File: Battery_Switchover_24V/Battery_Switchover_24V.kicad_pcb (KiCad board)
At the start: 4 copper layers, 198.6 x 89 mm, 194 parts, among them J1 USB_C_Receptacle_USB2.0_14P, J10 ATX_2X3, J11 ATX_2X3, J12 ATX_2X3, J13 ATX_2X3, J14 M6, J15 M6, J2 M8, J4 M8, J5 M8, J6 Conn_01x08, J7 Conn_01x05, J8 ATX_2X3, J9 ATX_2X3, M1 Fan, Q1 PZT2222AT1G, Q10 FDBL86066-F085, Q11 BC817, Q2 PJD50N10AL_L2, Q3 PJD50N10AL_L2, Q4 FDBL86066-F085, Q5 FDBL86066-F085, Q6 FDBL86066-F085, Q7 FDBL86066-F085, Q8 FDBL86066-F085, Q9 FDBL86066-F085, SW1 SW_Push, SW2 SW_Push, SW3 SW_Push, U1 LM25117PSQE_NOPB, U10 LPC11U67JBD48, U12 L5973D, U13 AMS1117-3.3, U14 OPA2197xD, U15 IRS21867S, U16 LM74610QDGKRQ1, U17 IRS21867S, U18 LM60CIM3_NOPB, U2 ACS71240LLCBTR-010B3, U3 IRS21867S, U4 ACS71240LLCBTR-010B3, U5 ACS71240LLCBTR-010B3, U6 LM74610QDGKRQ1, U7 ACS71240LLCBTR-010B3, U8 ADS7830IPWR, U9 LMV321

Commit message: Board turned to horizontal
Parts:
- removed C14: 10uF, Capacitor_SMD:C_1206_3216Metric
- removed C15: 100nF, Capacitor_SMD:C_1206_3216Metric
- removed C28: 330uF, Capacitor_SMD:CP_Elec_8x10
- removed C45: 100nF, Capacitor_SMD:C_0603_1608Metric
- added C67: 10uF 50V X7R, Capacitor_SMD:C_1206_3216Metric, F.Cu at (92.8, 98.3)
- added C68: 10uF 16V X7R, Capacitor_SMD:C_1206_3216Metric, F.Cu at (99.7, 74.4)
- added C69: 10uF 16V X7R, Capacitor_SMD:C_1206_3216Metric, F.Cu at (102.1, 74.4)
- added C70: 10uF 50V X7R, Capacitor_SMD:C_1206_3216Metric, F.Cu at (231.5, 134.6)
- added C71: 10uF 50V X7R, Capacitor_SMD:C_1206_3216Metric, F.Cu at (228.2, 134.6)
- added C72: 10uF 50V X7R, Capacitor_SMD:C_1206_3216Metric, F.Cu at (224.8, 134.6)
- added C73: 10uF 50V X7R, Capacitor_SMD:C_1206_3216Metric, F.Cu at (221.4, 134.6)
- added J3: Conn_01x03, Connector_Phoenix_MC:PhoenixContact_MCV_1,5_3-G-3.5_1x03_P3.50mm_Vertical, F.Cu at (162.2, 155.4)
- BZ1, D16, D2, D4, D5, J2, J4, J5: moved to F.Cu
- C33: value 1nF -> 10uF 50V X7R; footprint Capacitor_SMD:C_0402_1005Metric -> Capacitor_SMD:C_1206_3216Metric
- C34: value 10nF -> 10uF 50V X7R; footprint Capacitor_SMD:C_0603_1608Metric -> Capacitor_SMD:C_1206_3216Metric
- C35: value 100nF -> 10uF 50V X7R; footprint Capacitor_SMD:C_0603_1608Metric -> Capacitor_SMD:C_1206_3216Metric
- C36: value 1nF -> 100nF
- C37, C38: footprint Capacitor_SMD:C_0402_1005Metric -> Capacitor_SMD:C_0603_1608Metric
- C39: value 100nF -> 100nF 16V; footprint Capacitor_SMD:C_0603_1608Metric -> Capacitor_SMD:C_1206_3216Metric
- C41: value 100nF -> 10uF 16V X7R; footprint Capacitor_SMD:C_0603_1608Metric -> Capacitor_SMD:C_1206_3216Metric
- C42: footprint Capacitor_SMD:C_0603_1608Metric -> Capacitor_SMD:C_0805_2012Metric
- C9: footprint Capacitor_SMD:C_0603_1608Metric -> Capacitor_SMD:C_1206_3216Metric
- DS1: footprint LCD_OLED_I2C:LCD_OLED_128X64_1.3_I2C -> Connector_PinSocket_2.54mm:PinSocket_1x04_P2.54mm_Vertical
- J1: footprint USB_C_Vertical:GCT_USB4145-03-0170-C_REVA2 -> Connector_USB:USB_C_Receptacle_HRO_TYPE-C-31-M-12; moved to F.Cu
- J6: footprint TerminalBlock_Phoenix:TerminalBlock_Phoenix_PT-1,5-8-3.5-H_1x08_P3.50mm_Horizontal -> Connector_Phoenix_MC:PhoenixContact_MCV_1,5_8-G-3.5_1x08_P3.50mm_Vertical
- M1: footprint TerminalBlock_Phoenix:TerminalBlock_Phoenix_PT-1,5-2-3.5-H_1x02_P3.50mm_Horizontal -> Connector_Phoenix_MC:PhoenixContact_MCV_1,5_2-G-3.5_1x02_P3.50mm_Vertical
- SW1, SW2, SW3: footprint Button_Switch_SMD:SW_SPST_TL3305A -> Button_Switch_THT:SW_Tactile_SPST_Angled_PTS645Vx58-2LFS; moved to F.Cu
- moved C41 317.7 mm to (97.2, 74.3)
- moved C39 311.3 mm to (112.8, 74.5), turned to 90 degrees
- moved C36 307.4 mm to (120.0, 73.5)
- moved R18 307.2 mm to (91.1, 88.0)
- moved C35 299.7 mm to (92.8, 95.9)
- moved C33 297.1 mm to (98.0, 98.3), turned to 180 degrees
- moved C34 293.6 mm to (98.0, 95.9), turned to 180 degrees
- moved C38 288.6 mm to (100.2, 86.7)
- moved C37 285.8 mm to (100.2, 88.3)
- moved C42 281.5 mm to (115.4, 73.2), turned to 180 degrees
- moved R19 271.3 mm to (91.0, 91.8)
- moved U13 267.8 mm to (119.1, 79.8)
- moved R17 251.0 mm to (100.2, 90.0)
- moved D10 238.7 mm to (92.3, 81.2), turned to 90 degrees
- moved C32 227.2 mm to (105.9, 95.5)
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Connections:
- C41 pad 1: +5V -> GND
- C41 pad 2: GND -> +5V
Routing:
- net VOUT: track 394.1 -> 149.3 mm
- net VIN: track 56.7 -> 24.0 mm
- net VBATT: track 45.4 -> 21.0 mm
- net GND: track 9.65 -> 0.00 mm
- net Net-(Q2-S): track 10.5 -> 6.59 mm
- removed copper zone on F.Cu, net VBATT
- removed copper zone on B.Cu, net VOUT
- removed copper zone on F.Cu, net VOUT
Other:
- board size 198.6 x 89 mm -> 198.6 x 104.2 mm

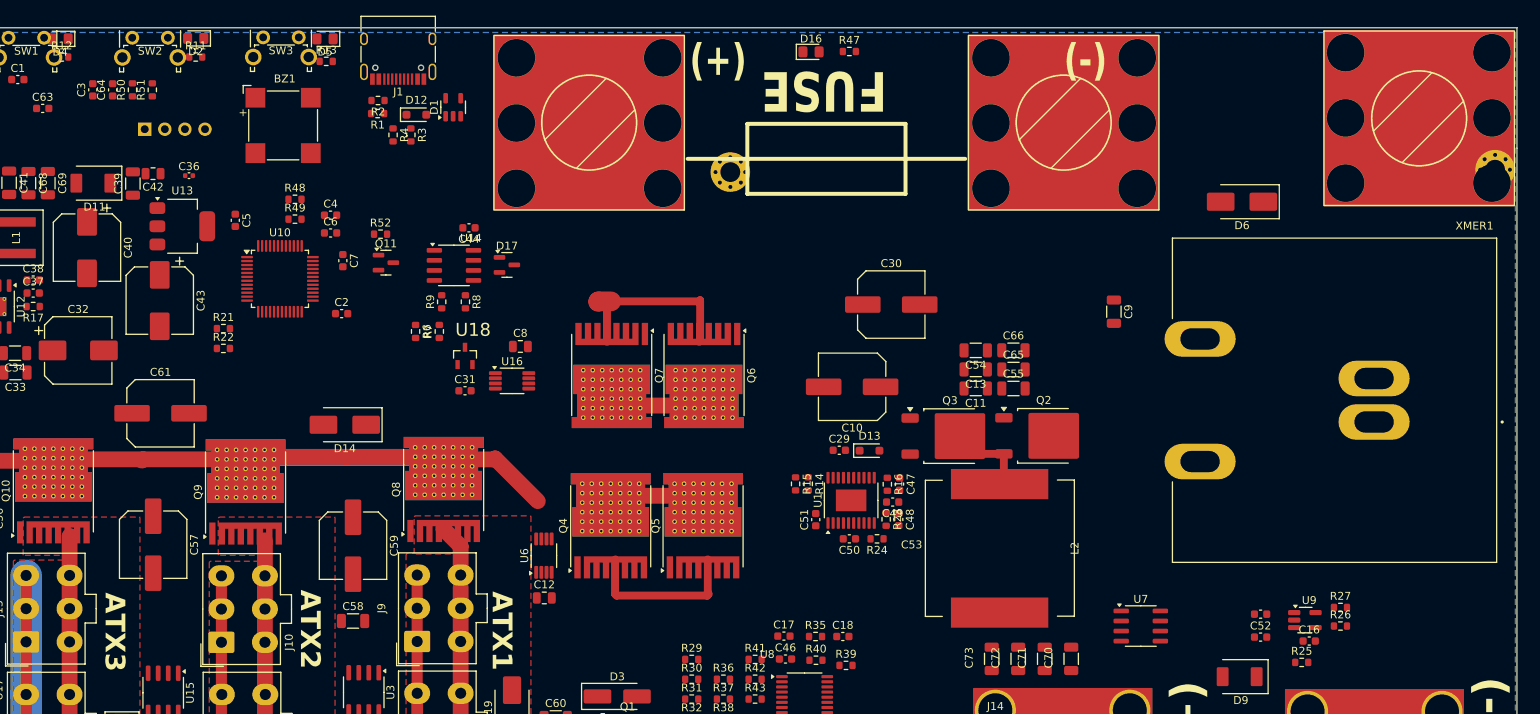
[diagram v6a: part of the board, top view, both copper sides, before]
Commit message: hiside load switch revised
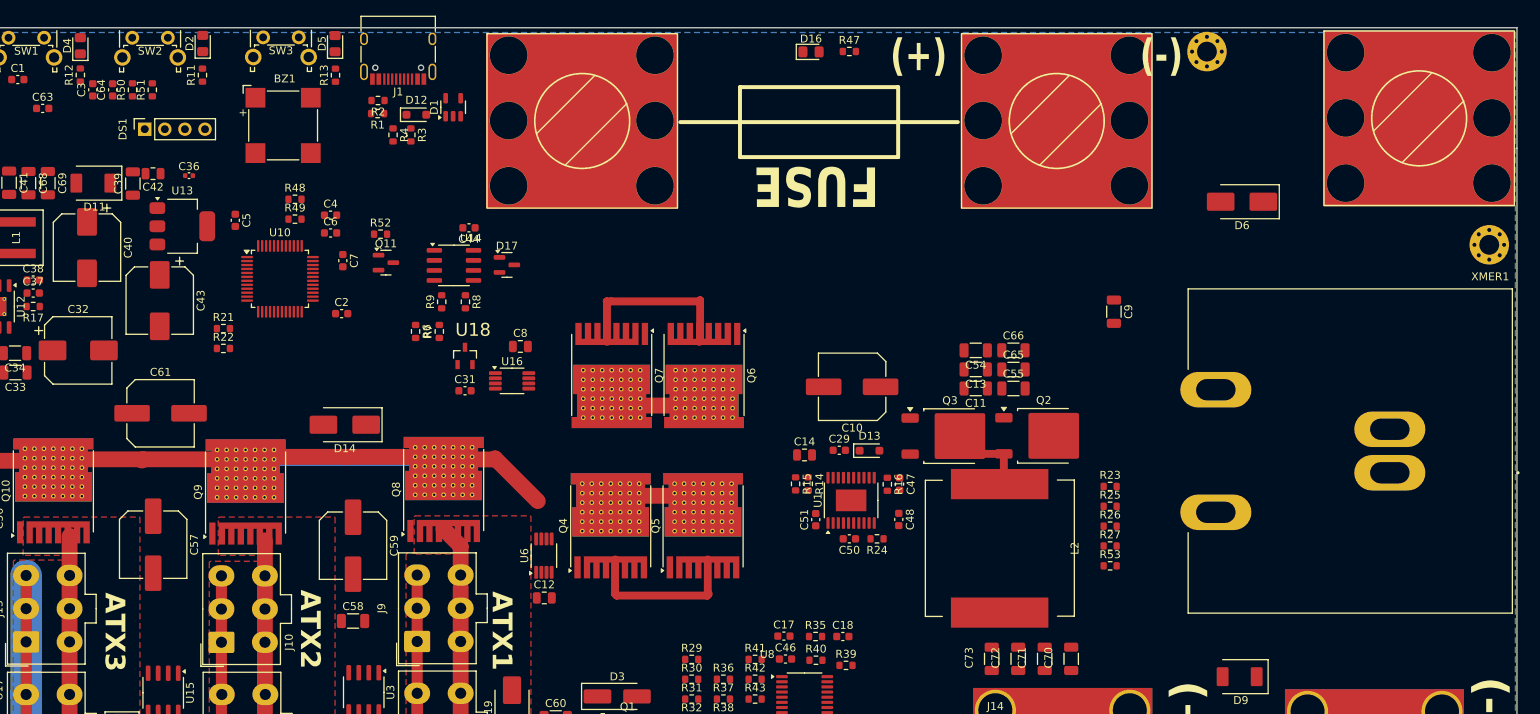
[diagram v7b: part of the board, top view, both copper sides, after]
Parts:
- removed C16, C49, C53: 100nF, Capacitor_SMD:C_0603_1608Metric
- removed C30: 330uF, Capacitor_SMD:C_Elec_8x10.2
- removed C52: 6nF, Capacitor_SMD:C_0603_1608Metric
- removed U7: ACS71240LLCBTR-010B3, Package_SO:SOIC-8_3.9x4.9mm_P1.27mm
- removed U9: LMV321, Package_TO_SOT_SMD:SOT-23-5_HandSoldering
- added C14: 1uF, Capacitor_SMD:C_0805_2012Metric, F.Cu at (197.8, 108.8)
- added R53: 5mOhm, Resistor_SMD:R_0603_1608Metric, F.Cu at (236.4, 122.8)
- C29, C50: value 100nF -> 0.47uF
- C47: value 100nF -> 1500pF
- C48: value 100nF -> 0.022uF
- DS1: moved to F.Cu
- R14, R16: value 7.5K -> 100K
- R15: value 7.5K -> 15K
- R23, R26: value 7.5K -> 3.24K
- R24: value 7.5K -> 22.1K
- R25: value 7.5K -> 2.37K
- R27: value 7.5K -> 332R
- moved J5 81.2 mm to (160.4, 58.2), turned to 0 degrees
- moved H6 62.2 mm to (248.7, 57.8)
- moved J2 43.9 mm to (220.4, 58.2), turned to 0 degrees
- moved R26 31.7 mm to (236.4, 117.8)
- moved R25 31.2 mm to (236.4, 115.3)
- moved R27 30.1 mm to (236.4, 120.3)
- moved R23 28.6 mm to (236.4, 112.8), turned to 0 degrees
- moved H4 9.52 mm to (284.4, 82.2)
- moved XMER1 6.72 mm to (266.8, 108.3)
- moved R12 3.28 mm to (106.2, 60.7), turned to 90 degrees
- moved D4 2.71 mm to (106.2, 57.0), turned to 90 degrees
- moved R11 2.44 mm to (121.7, 60.7), turned to 90 degrees
- moved R13 2.11 mm to (138.5, 60.8), turned to 90 degrees
- moved D5 1.41 mm to (138.4, 56.8), turned to 90 degrees
- moved D2 1.09 mm to (121.7, 56.7), turned to 90 degrees
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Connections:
- C29 pad 2: Net-(Q2-S) -> /Charge Control/SW
- C48 pad 2: Net-(C48-Pad2) -> Net-(U1-COMP)
- C70 pad 1: Net-(U7-IP+1) -> VBATT
- C71 pad 1: Net-(U7-IP+1) -> VBATT
- C72 pad 1: Net-(U7-IP+1) -> VBATT
- C73 pad 1: Net-(U7-IP+1) -> VBATT
- L2 pad 1: Net-(Q2-S) -> /Charge Control/SW
- L2 pad 2: Net-(U7-IP+1) -> VBATT
- Q2 pad 3: Net-(Q2-S) -> /Charge Control/SW
- Q3 pad 2: Net-(Q2-S) -> /Charge Control/SW
- Q3 pad 3: GND -> Net-(Q3-S)
- R16 pad 2: unconnected-(R16-Pad2) -> /Charge Control/SW
- R23 pad 1: Net-(U1-COMP) -> /Charge Control/FB
- R23 pad 2: Net-(C48-Pad2) -> Net-(U1-CM)
- R25 pad 1: BATT_CURRENT -> GND
- R25 pad 2: Net-(U9-+) -> /Charge Control/FB
- R26 pad 1: Net-(U9-+) -> Net-(U1-VCCDIS)
- R26 pad 2: GND -> VBATT
- R27 pad 1: Net-(U9-+) -> GND
- R27 pad 2: GND -> Net-(U1-VCCDIS)
- U1 pad 10: unconnected-(U1-CM-Pad10) -> Net-(U1-CM)
- U1 pad 12: unconnected-(U1-CS-Pad12) -> Net-(Q3-S)
- U1 pad 13: unconnected-(U1-CSG-Pad13) -> GND
- U1 pad 17: Net-(Q2-S) -> /Charge Control/SW
- U1 pad 7: unconnected-(U1-VCCDIS-Pad7) -> Net-(U1-VCCDIS)
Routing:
- net Net-(Q2-S): track 6.59 -> 0.00 mm
- net /Charge Control/SW: track 0.00 -> 6.59 mm
- net VIN: track 24.0 -> 22.3 mm
